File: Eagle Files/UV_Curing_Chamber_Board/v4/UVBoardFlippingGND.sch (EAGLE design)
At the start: 29 parts, among them IC1 7805T, IC2 L293D, T1 RFP30N06LE, T2 RFP30N06LE

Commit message: Updated V4
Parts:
- C1, C4, C5, C6, C7: device rcl:C-EU075-063X106 -> rcl:C-EUC0603
- C2, C3: device rcl:CPOL-USE1.8-4 -> rcl:C-EUC1206
- R1, R2, R3, R5: device rcl:R-US_0207/10 -> rcl:R-US_R0805
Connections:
- net +5V: now also C3.1; no longer C3.+
- net GND: now also C2.2, C3.2; no longer C2.-, C3.-
- net V+: now also C2.1; no longer C2.+
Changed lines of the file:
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@@
 <part name="LIGHTS" library="con-jack" library_urn="urn:adsk.eagle:library:154" deviceset="JACK-PLUG" device="0" package3d_urn="urn:adsk.eagle:package:7492/1"/>
 <part name="IC1" library="linear" library_urn="urn:adsk.eagle:library:262" deviceset="78*" device="T" package3d_urn="urn:adsk.eagle:package:16414/1" technology="05"/>
-<part name="C2" library="rcl" library_urn="urn:adsk.eagle:library:334" deviceset="CPOL-US" device="E1.8-4" package3d_urn="urn:adsk.eagle:package:23336/2" value="10uF"/>
-<part name="C3" library="rcl" library_urn="urn:adsk.eagle:library:334" deviceset="CPOL-US" device="E1.8-4" package3d_urn="urn:adsk.eagle:package:23336/2" value="10uF"/>
+<part name="C2" library="rcl" library_urn="urn:adsk.eagle:library:334" deviceset="C-EU" device="C1206" package3d_urn="urn:adsk.eagle:package:23618/2" value="10uF"/>
+<part name="C3" library="rcl" library_urn="urn:adsk.eagle:library:334" deviceset="C-EU" device="C1206" package3d_urn="urn:adsk.eagle:package:23618/2" value="10uF"/>
 <part name="T2" library="RFP30N06LE" deviceset="RFP30N06LE" device=""/>
 <part name="T1" library="RFP30N06LE" deviceset="RFP30N06LE" device=""/>
@@
 <part name="IC2" library="st-microelectronics" library_urn="urn:adsk.eagle:library:368" deviceset="L293D" device="" package3d_urn="urn:adsk.eagle:package:26820/1"/>
 <part name="U$1" library="ESP32-DEVKITC" deviceset="ESP32DEVKITC" device=""/>
-<part name="R5" library="rcl" library_urn="urn:adsk.eagle:library:334" deviceset="R-US_" device="0207/10" package3d_urn="urn:adsk.eagle:package:23491/1" value="10k"/>
-<part name="R1" library="rcl" library_urn="urn:adsk.eagle:library:334" deviceset="R-US_" device="0207/10" package3d_urn="urn:adsk.eagle:package:23491/1" value="220"/>
-<part name="R2" library="rcl" library_urn="urn:adsk.eagle:library:334" deviceset="R-US_" device="0207/10" package3d_urn="urn:adsk.eagle:package:23491/1" value="10k"/>
-<part name="R3" library="rcl" library_urn="urn:adsk.eagle:library:334" deviceset="R-US_" device="0207/10" package3d_urn="urn:adsk.eagle:package:23491/1" value="220"/>
-<part name="C1" library="rcl" library_urn="urn:adsk.eagle:library:334" deviceset="C-EU" device="075-063X106" package3d_urn="urn:adsk.eagle:package:23678/1" value=".1uF"/>
+<part name="R5" library="rcl" library_urn="urn:adsk.eagle:library:334" deviceset="R-US_" device="R0805" package3d_urn="urn:adsk.eagle:package:23553/2" value="10k"/>
+<part name="R1" library="rcl" library_urn="urn:adsk.eagle:library:334" deviceset="R-US_" device="R0805" package3d_urn="urn:adsk.eagle:package:23553/2" value="220"/>
+<part name="R2" library="rcl" library_urn="urn:adsk.eagle:library:334" deviceset="R-US_" device="R0805" package3d_urn="urn:adsk.eagle:package:23553/2" value="10k"/>
+<part name="R3" library="rcl" library_urn="urn:adsk.eagle:library:334" deviceset="R-US_" device="R0805" package3d_urn="urn:adsk.eagle:package:23553/2" value="220"/>
+<part name="C1" library="rcl" library_urn="urn:adsk.eagle:library:334" deviceset="C-EU" device="C0603" package3d_urn="urn:adsk.eagle:package:23616/2" value=".1uF"/>
 <part name="P+1" library="supply1" library_urn="urn:adsk.eagle:library:371" deviceset="+5V" device=""/>
 <part name="P+2" library="supply1" library_urn="urn:adsk.eagle:library:371" deviceset="+5V" device=""/>
@@
 <part name="+3V5" library="supply1" library_urn="urn:adsk.eagle:library:371" deviceset="+3V3" device=""/>
 <part name="+3V6" library="supply1" library_urn="urn:adsk.eagle:library:371" deviceset="+3V3" device=""/>
-<part name="C4" library="rcl" library_urn="urn:adsk.eagle:library:334" deviceset="C-EU" device="075-063X106" package3d_urn="urn:adsk.eagle:package:23678/1" value="0.1u"/>
-<part name="C5" library="rcl" library_urn="urn:adsk.eagle:library:334" deviceset="C-EU" device="075-063X106" package3d_urn="urn:adsk.eagle:package:23678/1" value="0.1u"/>
-<part name="C6" library="rcl" library_urn="urn:adsk.eagle:library:334" deviceset="C-EU" device="075-063X106" package3d_urn="urn:adsk.eagle:package:23678/1" value="0.1u"/>
-<part name="C7" library="rcl" library_urn="urn:adsk.eagle:library:334" deviceset="C-EU" device="075-063X106" package3d_urn="urn:adsk.eagle:package:23678/1" value="0.1u"/>
+<part name="C4" library="rcl" library_urn="urn:adsk.eagle:library:334" deviceset="C-EU" device="C0603" package3d_urn="urn:adsk.eagle:package:23616/2" value="0.1u"/>
+<part name="C5" library="rcl" library_urn="urn:adsk.eagle:library:334" deviceset="C-EU" device="C0603" package3d_urn="urn:adsk.eagle:package:23616/2" value="0.1u"/>
+<part name="C6" library="rcl" library_urn="urn:adsk.eagle:library:334" deviceset="C-EU" device="C0603" package3d_urn="urn:adsk.eagle:package:23616/2" value="0.1u"/>
+<part name="C7" library="rcl" library_urn="urn:adsk.eagle:library:334" deviceset="C-EU" device="C0603" package3d_urn="urn:adsk.eagle:package:23616/2" value="0.1u"/>
 <part name="GND6" library="supply1" library_urn="urn:adsk.eagle:library:371" deviceset="GND" device=""/>
 <part name="GND18" library="supply1" library_urn="urn:adsk.eagle:library:371" deviceset="GND" device=""/>
@@
 <pinref part="GND2" gate="1" pin="GND"/>
 <wire x1="101.6" y1="149.86" x2="101.6" y2="142.24" width="0.1524" layer="91"/>
-<pinref part="C2" gate="G$1" pin="-"/>
+<pinref part="C2" gate="G$1" pin="2"/>
 <wire x1="88.9" y1="147.32" x2="88.9" y2="142.24" width="0.1524" layer="91"/>
 <wire x1="101.6" y1="142.24" x2="88.9" y2="142.24" width="0.1524" layer="91"/>
 <junction x="101.6" y="142.24"/>
-<pinref part="C3" gate="G$1" pin="-"/>
+<pinref part="C3" gate="G$1" pin="2"/>
 <wire x1="114.3" y1="144.78" x2="114.3" y2="142.24" width="0.1524" layer="91"/>
 <wire x1="101.6" y1="142.24" x2="114.3" y2="142.24" width="0.1524" layer="91"/>
@@
 <net name="+5V" class="0">
 <segment>
-<pinref part="C3" gate="G$1" pin="+"/>
+<pinref part="C3" gate="G$1" pin="1"/>
 <pinref part="IC1" gate="A1" pin="VO"/>
 <wire x1="111.76" y1="157.48" x2="114.3" y2="157.48" width="0.1524" layer="91"/>
@@
 <wire x1="78.74" y1="157.48" x2="88.9" y2="157.48" width="0.1524" layer="91"/>
 <pinref part="POWER_SWITCH" gate="G$1" pin="2"/>
-<pinref part="C2" gate="G$1" pin="+"/>
+<pinref part="C2" gate="G$1" pin="1"/>
 <wire x1="88.9" y1="157.48" x2="91.44" y2="157.48" width="0.1524" layer="91"/>
 <wire x1="88.9" y1="154.94" x2="88.9" y2="157.48" width="0.1524" layer="91"/>

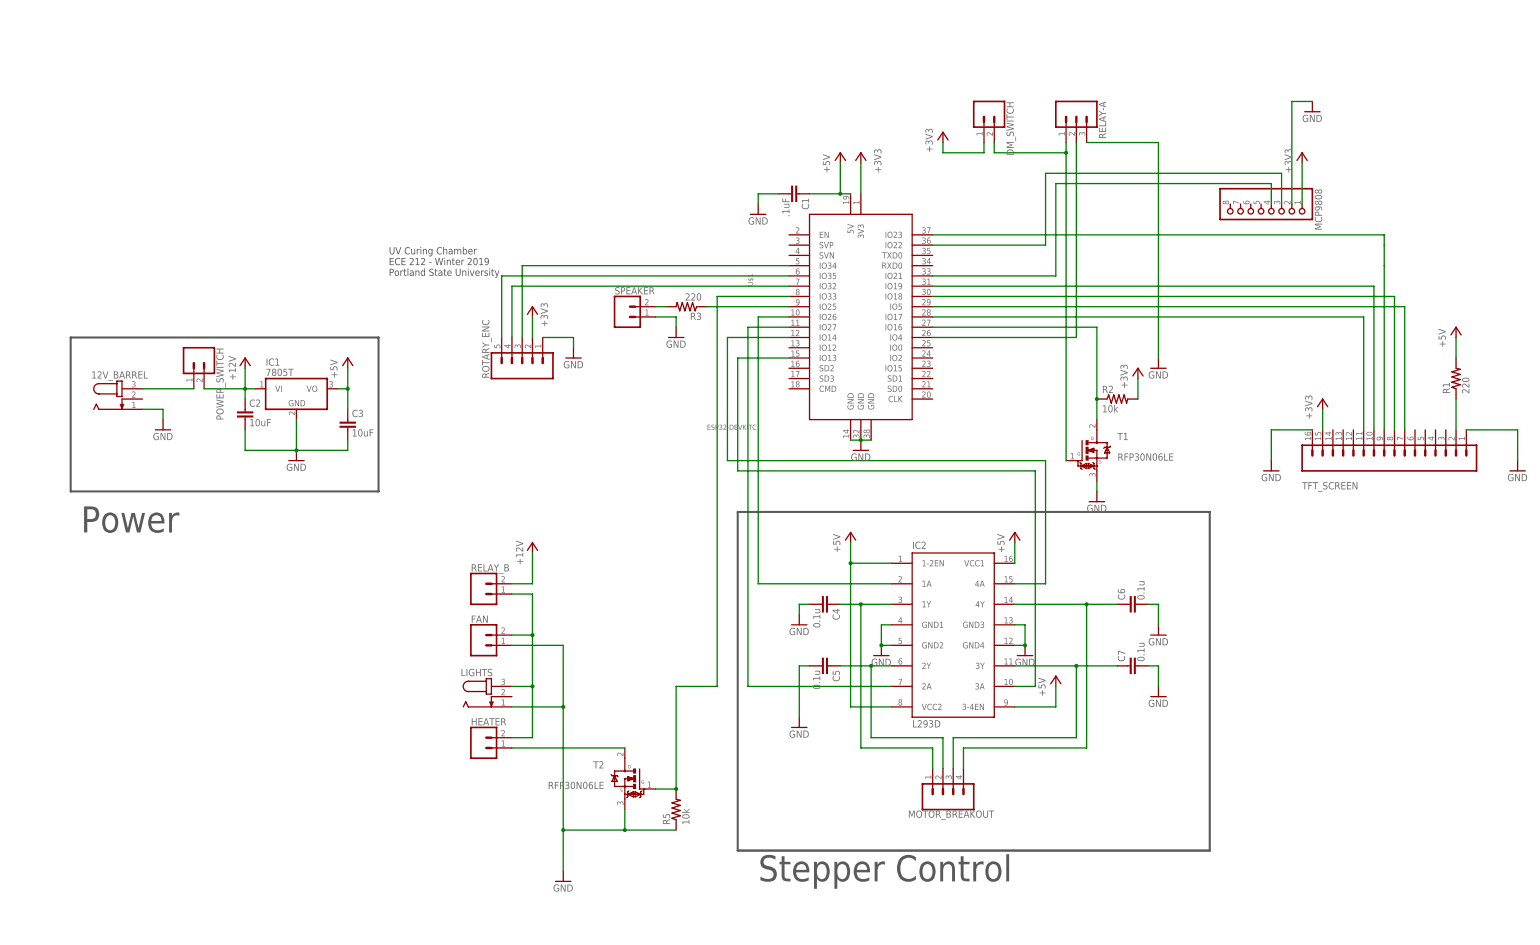
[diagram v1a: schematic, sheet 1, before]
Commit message: V4 board now has relay circuit on board.
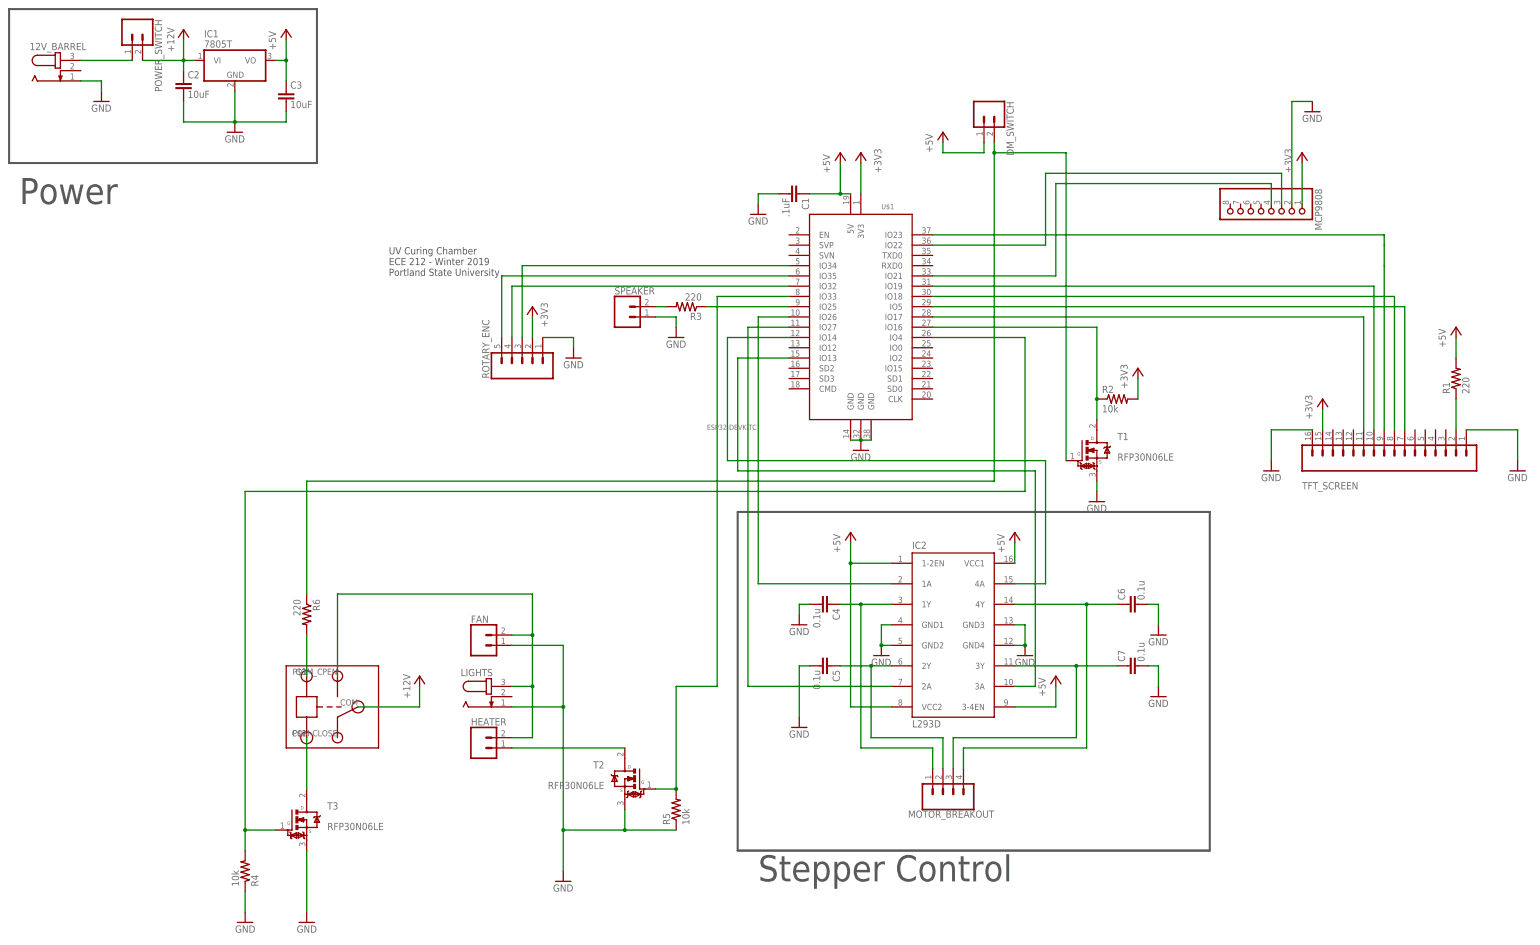
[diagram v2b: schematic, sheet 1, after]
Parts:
- removed RELAY-A: (no value), SparkFun-Connectors:CONN_03-SCREW-5MM
- removed RELAY_B: (no value), SparkFun-Connectors:CONN_025MM
- added R4: 10k, rcl:R-US_R0805
- added R6: 220, rcl:R-US_R0805
- added T3: RFP30N06LE, RFP30N06LE:RFP30N06LE
- added U$2: RELAY, RELAY:RELAY
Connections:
- new net N$31: T3.D, U$2.GND
- new net N$32: R6.2, U$2.IN
- net +3V3: no longer DM_SWITCH.1
- net +5V: now also DM_SWITCH.1
- net GND: now also R4.1, T3.S; no longer RELAY-A.3
- net N$16: now also R4.2, T3.G; no longer RELAY-A.2
- net N$28: now also U$2.COM-OPEN; no longer RELAY_B.1
- net N$8: now also R6.1; no longer RELAY-A.1
- net V+: now also U$2.COM; no longer RELAY_B.2
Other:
- moved on the sheet: 12V_BARREL, C2, C3, IC1, POWER_SWITCH

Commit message: SMD revisions for the PCB
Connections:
- net V+ renamed ASDSFA
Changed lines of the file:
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@@
 <?xml version="1.0" encoding="utf-8"?>
 <!DOCTYPE eagle SYSTEM "eagle.dtd">
-<eagle version="9.5.1">
+<eagle version="9.4.0">
 <drawing>
 <settings>
@@
 </segment>
 </net>
-<net name="V+" class="1">
+<net name="ASDSFA" class="1">
 <segment>
 <pinref part="IC1" gate="A1" pin="VI"/>

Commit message: Added comments about switching out the transistors in the V4 schematic.
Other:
- note added: "May switch out with a TN0702 so the threshhold voltage is lower because the IRF530N has a Vth between 2 and 4 volts so it might not be triggering."
- note added: "We need to switch out this transistor because it needs a max current of at least 12.5A and the threshold voltage was too high."
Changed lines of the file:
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@@
 <?xml version="1.0" encoding="utf-8"?>
 <!DOCTYPE eagle SYSTEM "eagle.dtd">
-<eagle version="9.4.0">
+<eagle version="9.5.1">
 <drawing>
 <settings>
@@
 <wire x1="106.68" y1="251.46" x2="30.48" y2="251.46" width="0.508" layer="97"/>
 <text x="33.02" y="203.2" size="6.4516" layer="97">Power</text>
+<text x="114.3" y="33.02" size="1.778" layer="91">May switch out with a TN0702
+so the threshhold voltage is lower
+because the IRF530N has a Vth
+between 2 and 4 volts so it might
+not be triggering.</text>
+<text x="175.26" y="30.48" size="1.778" layer="91">We need to switch out this
+transistor because it needs a
+max current of at least 12.5A
+and the threshold voltage was
+too high.</text>
 </plain>
 <instances>
